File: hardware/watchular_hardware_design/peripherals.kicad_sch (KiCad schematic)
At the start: 8 parts, among them Q1 BC817

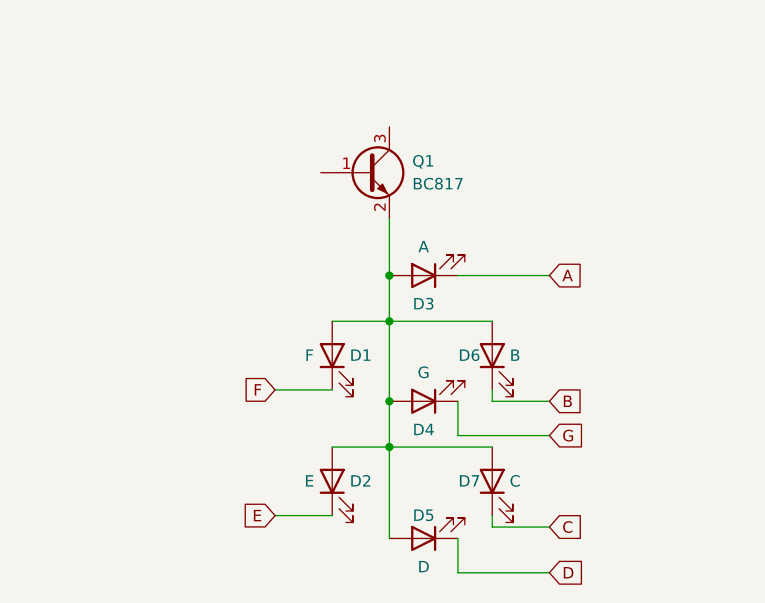
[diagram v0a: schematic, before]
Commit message: Added current limiting resistors and connected to MCU.
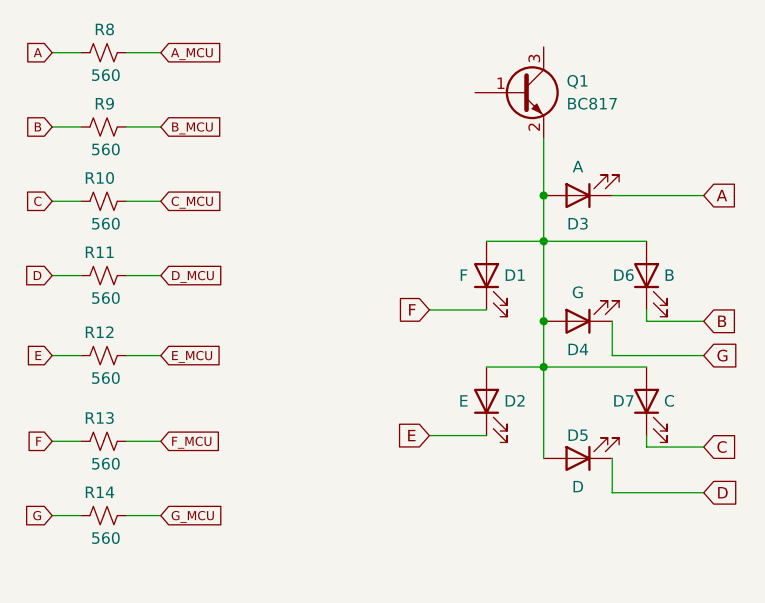
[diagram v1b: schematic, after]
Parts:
- added R10, R11, R12, R13, R14, R8, R9: 560, Resistor_SMD:R_0402_1005Metric_Pad0.72x0.64mm_HandSolder, symbol Device:R_Small_US
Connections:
- net A: now also R8.1
- net B: now also R9.1
- net C: now also R10.1
- net D: now also R11.1
- net E: now also R12.1
- net F: now also R13.1
- net G: now also R14.1
- new net A_MCU: R8.2
- new net B_MCU: R9.2
- new net C_MCU: R10.2
- new net D_MCU: R11.2
- new net E_MCU: R12.2
- new net F_MCU: R13.2
- new net G_MCU: R14.2
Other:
- moved on the sheet: D1, D2, D3, D4, D5, D6, D7, Q1

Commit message: Added components for 4 digits.
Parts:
- added D? (x3): F, LED_SMD:LED_0603_1608Metric, symbol Device:LED
- added D? (x3): E, LED_SMD:LED_0603_1608Metric, symbol Device:LED
- added D? (x3): G, LED_SMD:LED_0603_1608Metric, symbol Device:LED
- added D? (x3): D, LED_SMD:LED_0603_1608Metric, symbol Device:LED
- added D? (x3): B, LED_SMD:LED_0603_1608Metric, symbol Device:LED
- added D? (x3): A, LED_SMD:LED_0603_1608Metric, symbol Device:LED
- added D? (x3): C, LED_SMD:LED_0603_1608Metric, symbol Device:LED
- added Q? (x3): BC817, Package_TO_SOT_SMD:SOT-23, symbol Transistor_BJT:BC817
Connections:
- net A: now also D?.1 (K), D?.1 (K), D?.1 (K)
- net B: now also D?.1 (K), D?.1 (K), D?.1 (K)
- net C: now also D?.1 (K), D?.1 (K), D?.1 (K)
- net D: now also D?.1 (K), D?.1 (K), D?.1 (K)
- net E: now also D?.1 (K), D?.1 (K), D?.1 (K)
- net F: now also D?.1 (K), D?.1 (K), D?.1 (K)
- net G: now also D?.1 (K), D?.1 (K), D?.1 (K)
- new net: D?.2 (A), D?.2 (A), D?.2 (A), D?.2 (A), D?.2 (A), D?.2 (A), D?.2 (A), Q?.2 (E) (x3)

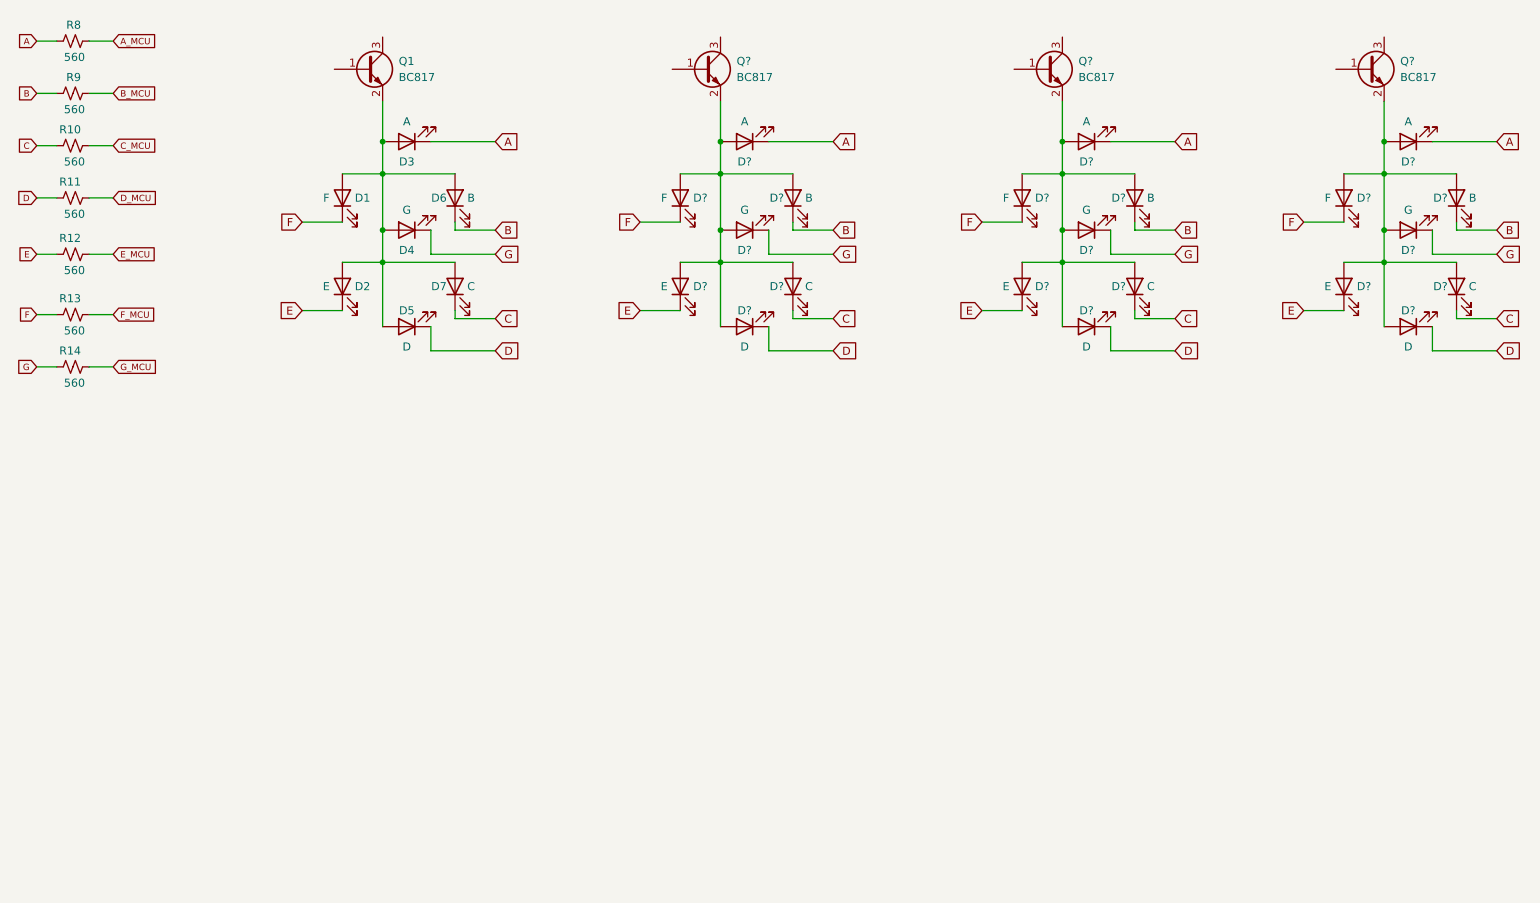
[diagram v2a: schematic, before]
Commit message: Added MOSFET-BSS123 to the project.
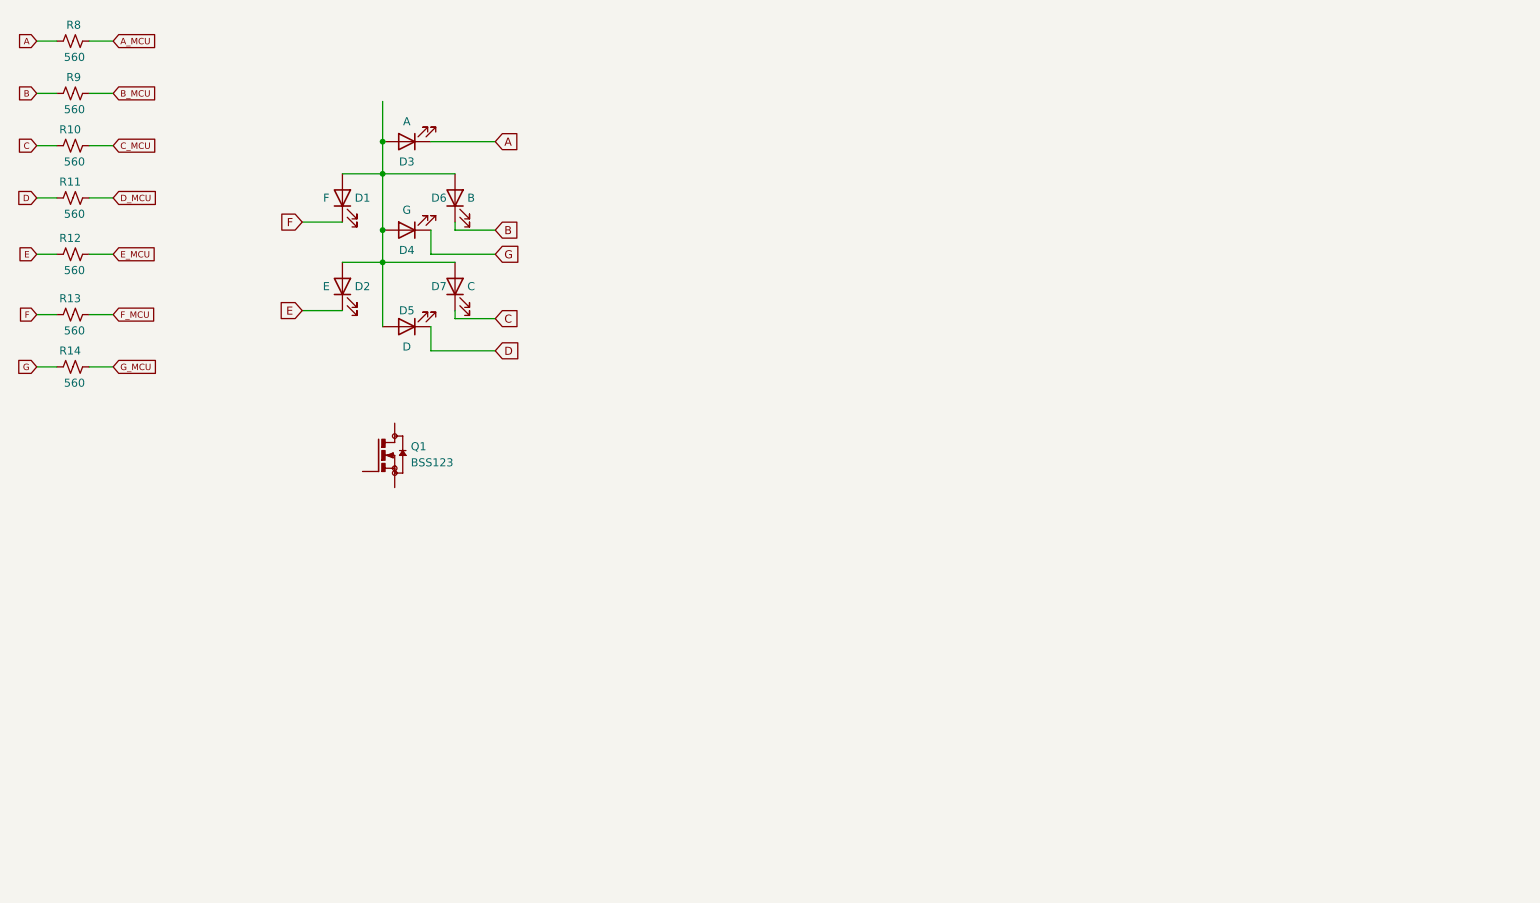
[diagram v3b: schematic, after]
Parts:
- removed D? (x3): F, LED_SMD:LED_0603_1608Metric, symbol Device:LED
- removed D? (x3): E, LED_SMD:LED_0603_1608Metric, symbol Device:LED
- removed D? (x3): G, LED_SMD:LED_0603_1608Metric, symbol Device:LED
- removed D? (x3): D, LED_SMD:LED_0603_1608Metric, symbol Device:LED
- removed D? (x3): B, LED_SMD:LED_0603_1608Metric, symbol Device:LED
- removed D? (x3): A, LED_SMD:LED_0603_1608Metric, symbol Device:LED
- removed D? (x3): C, LED_SMD:LED_0603_1608Metric, symbol Device:LED
- removed Q1, Q? (x3): BC817, Package_TO_SOT_SMD:SOT-23, symbol Transistor_BJT:BC817
- added Q1: BSS123, MOSFET-BSS123:SOT23, symbol BSS123:BSS123

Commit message: Added MOSFET to all 4 digits.
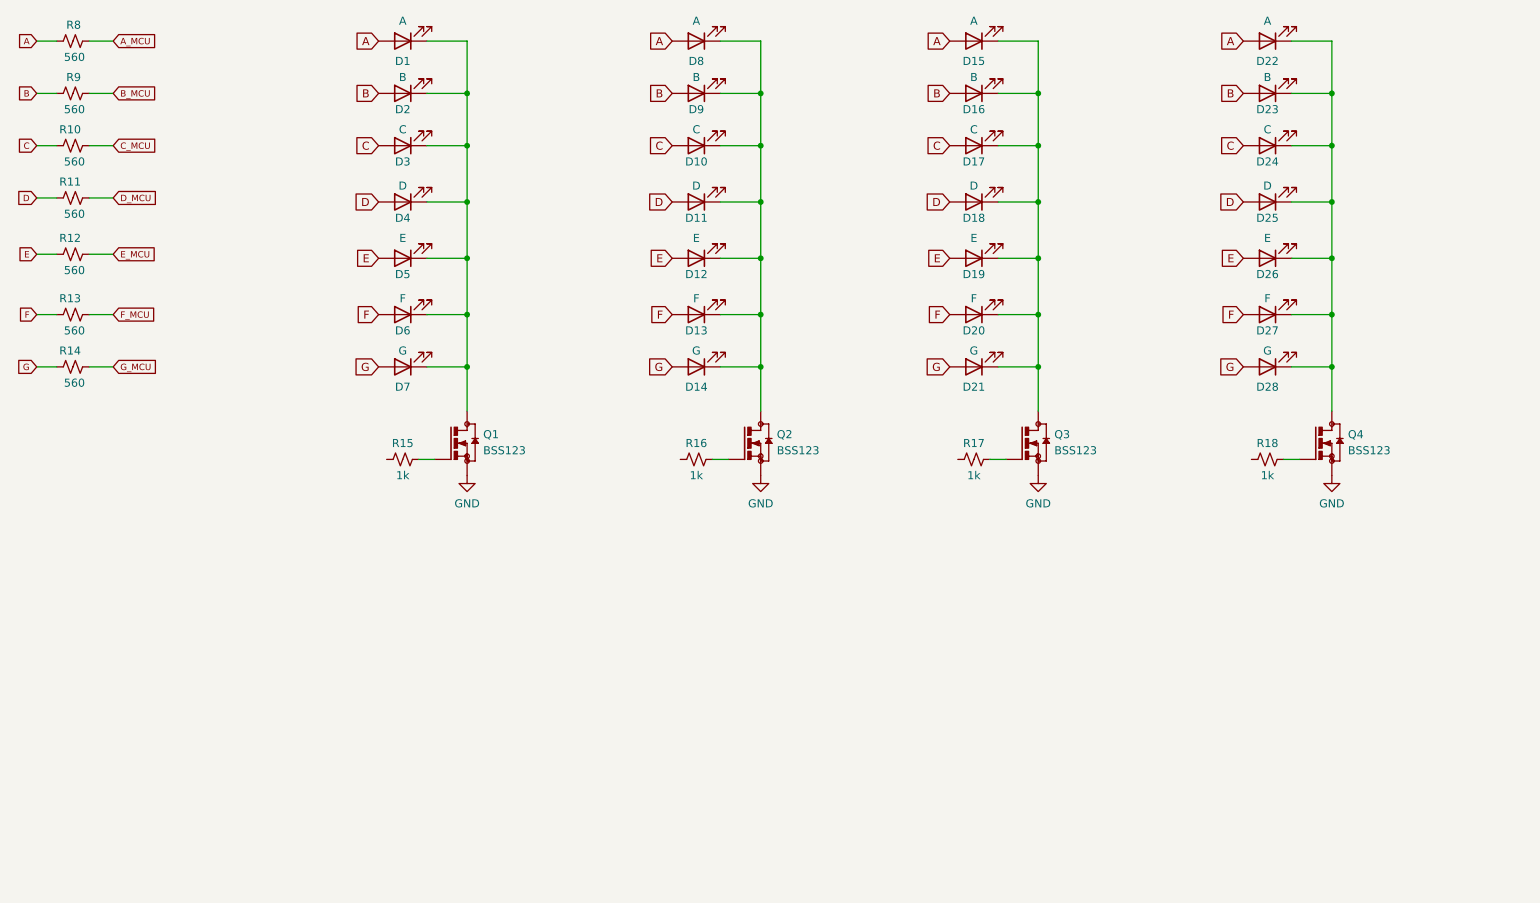
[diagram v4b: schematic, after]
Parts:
- added D10, D17, D24: C, LED_SMD:LED_0603_1608Metric, symbol Device:LED
- added D11, D18, D25: D, LED_SMD:LED_0603_1608Metric, symbol Device:LED
- added D12, D19, D26: E, LED_SMD:LED_0603_1608Metric, symbol Device:LED
- added D13, D20, D27: F, LED_SMD:LED_0603_1608Metric, symbol Device:LED
- added D14, D21, D28: G, LED_SMD:LED_0603_1608Metric, symbol Device:LED
- added D15, D22, D8: A, LED_SMD:LED_0603_1608Metric, symbol Device:LED
- added D16, D23, D9: B, LED_SMD:LED_0603_1608Metric, symbol Device:LED
- added Q2, Q3, Q4: BSS123, MOSFET-BSS123:SOT23, symbol BSS123:BSS123
- added R15, R16, R17, R18: 1k, Resistor_SMD:R_0402_1005Metric_Pad0.72x0.64mm_HandSolder, symbol Device:R_Small_US
- renumbered D3 to D1, D6 to D2, D7 to D3, D5 to D4, D2 to D5, D1 to D6, D4 to D7
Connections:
- net A: now also D1.2 (A), D15.2 (A), D22.2 (A), D8.2 (A); no longer D1.1 (K)
- net B: now also D2.2 (A), D16.2 (A), D23.2 (A), D9.2 (A); no longer D2.1 (K)
- net C: now also D3.2 (A), D10.2 (A), D17.2 (A), D24.2 (A); no longer D3.1 (K)
- net D: now also D4.2 (A), D11.2 (A), D18.2 (A), D25.2 (A); no longer D4.1 (K)
- net E: now also D5.2 (A), D12.2 (A), D19.2 (A), D26.2 (A); no longer D5.1 (K)
- net F: now also D6.2 (A), D13.2 (A), D20.2 (A), D27.2 (A); no longer D6.1 (K)
- net G: now also D7.2 (A), D14.2 (A), D21.2 (A), D28.2 (A); no longer D7.1 (K)
- net at Q1.1: now also R15.2
- net GND: now reaches Q1.2
- net GND: now also Q2.2, Q3.2, Q4.2
- net at Q1.3: now also D1.1 (K), D2.1 (K), D3.1 (K), D4.1 (K), D5.1 (K), D6.1 (K), D7.1 (K)
- new net: Q3.1, R17.2
- new net: D15.1 (K), D16.1 (K), D17.1 (K), D18.1 (K), D19.1 (K), D20.1 (K), D21.1 (K), Q3.3
- new net: D22.1 (K), D23.1 (K), D24.1 (K), D25.1 (K), D26.1 (K), D27.1 (K), D28.1 (K), Q4.3
- new net: D10.1 (K), D11.1 (K), D12.1 (K), D13.1 (K), D14.1 (K), D8.1 (K), D9.1 (K), Q2.3
- new net: Q4.1, R18.2
- new net: Q2.1, R16.2
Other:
- moved on the sheet: D1, D2, D3, D4, D5, D6, D7, Q1
